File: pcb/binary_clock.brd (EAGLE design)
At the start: 100 x 80 mm, 18 parts

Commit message: PCB almost done.
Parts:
- added C1: (no value), rcl:C0603K
- added R1, R2: (no value), rcl:R0603
- added S1: SET, SparkFun-Switches:TACTILE_SWITCH_SMD_5.2MM
- moved U$1 62.1 mm to (17.8, 52.1), flipped to the bottom, turned to 90 degrees
- moved D11 38.1 mm to (14.0, 55.9), turned to 90 degrees
- moved D6 38.1 mm to (52.1, 55.9), turned to 90 degrees
- moved D10 22.9 mm to (21.6, 55.9), turned to 90 degrees
- moved D7 22.9 mm to (44.5, 55.9), turned to 90 degrees
- moved D4 7.62 mm to (44.5, 63.5)
- moved D2 7.62 mm to (29.2, 63.5)
- moved D1 7.62 mm to (21.6, 63.5)
- moved D3 7.62 mm to (36.8, 63.5)
- moved D5 7.62 mm to (52.1, 63.5)
- moved D8 7.62 mm to (36.8, 55.9), turned to 90 degrees
- moved D9 7.62 mm to (29.2, 55.9), turned to 90 degrees
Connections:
- new net LED_CK: R1.1, U$1.6
- new net LED_D: R2.1, U$1.5
- new net N$31: D17.P6
- new net N$32: U$1.1
- new net N$33: U$1.3
- new net N$34: D17.P5
- new net N$35: U$1.2
- new net N$36: U$1.7
- new net N$41: D1.P1, R2.2
- new net N$42: D1.P2, R1.2
- new net SW: S1.1, S1.2
- net +5V: now also C1.1
- net GND: now also C1.2, S1.3, S1.4
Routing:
- net GND: track 0.00 -> 110.6 mm, vias 0 -> 17
- net +5V: track 0.00 -> 63.3 mm, vias 0 -> 17
- net N$38: track 48.3 -> 10.9 mm
- net N$37: track 42.3 -> 16.3 mm
- net N$20: track 0.00 -> 10.9 mm
- net LED_CK: track 0.00 -> 8.92 mm
- net N$41: track 0.00 -> 6.81 mm, vias 0 -> 1
- net LED_D: track 0.00 -> 5.14 mm
- net N$19: track 0.00 -> 4.95 mm
- net N$42: track 0.00 -> 4.67 mm, vias 0 -> 1

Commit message: Switch connected
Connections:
- removed net N$36: U$1.7
- net SW: now also U$1.7
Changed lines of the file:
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@@
 <contactref element="U$1" pad="2"/>
-</signal>
-<signal name="N$36">
-<contactref element="U$1" pad="7"/>
 </signal>
 <signal name="LED_D">
@@
 <contactref element="S1" pad="2"/>
 <contactref element="S1" pad="1"/>
+<contactref element="U$1" pad="7"/>
 <wire x1="11.176" y1="65.405" x2="16.764" y2="65.405" width="0" layer="19" extent="1-1"/>
+<wire x1="20.934" y1="51.435" x2="16.764" y2="65.405" width="0" layer="19" extent="1-16"/>
 </signal>
 </signals>

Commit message: Routing done.
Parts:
- added R3: (no value), rcl:R0603
- added Y1: OSCILLATORSMD-5X3, SparkFun-Clocks:OSCILLATOR-SMD-5X3.2
- moved C1 12.8 mm to (16.8, 54.9)
- moved U$1 7.62 mm to (25.4, 52.1)
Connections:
- new net N$36: R3.2, S1.1, S1.2
- net +5V: now also Y1.4
- net GND: now also Y1.2
- net N$35: now also Y1.3
- net SW: now also R3.1; no longer S1.1, S1.2
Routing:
- net +5V: track 63.3 -> 144.7 mm, vias 17 -> 19
- net GND: track 110.6 -> 138.7 mm, vias 17 -> 18
- net N$36: track 0.00 -> 18.0 mm, vias 0 -> 1
- net SW: track 0.00 -> 13.3 mm
- net LED_CK: track 8.92 -> 14.2 mm
- net LED_D: track 5.14 -> 9.78 mm
- net N$35: track 0.00 -> 4.35 mm
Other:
- outline, holes or cut-outs redrawn
- board text added: "+"
- board text added: "-"

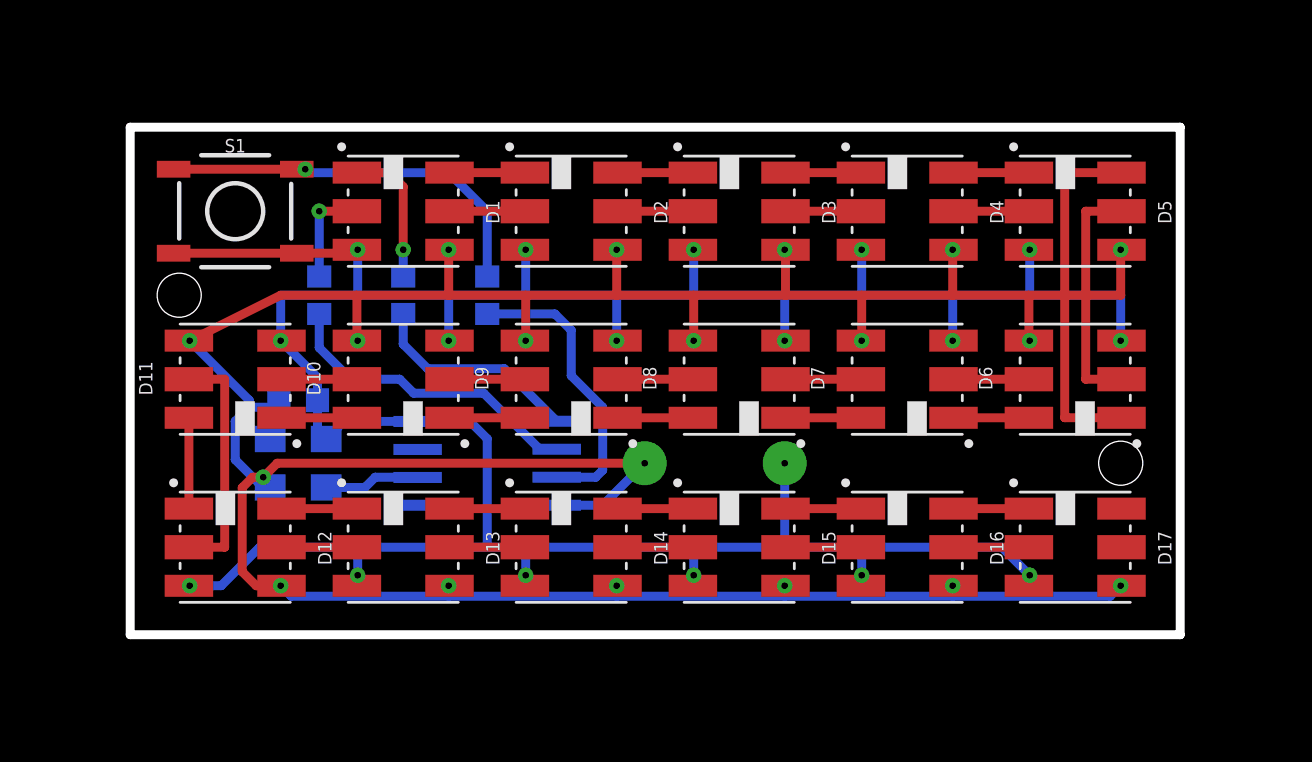
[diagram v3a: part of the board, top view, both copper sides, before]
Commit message: Silkscreen and resistor sizes
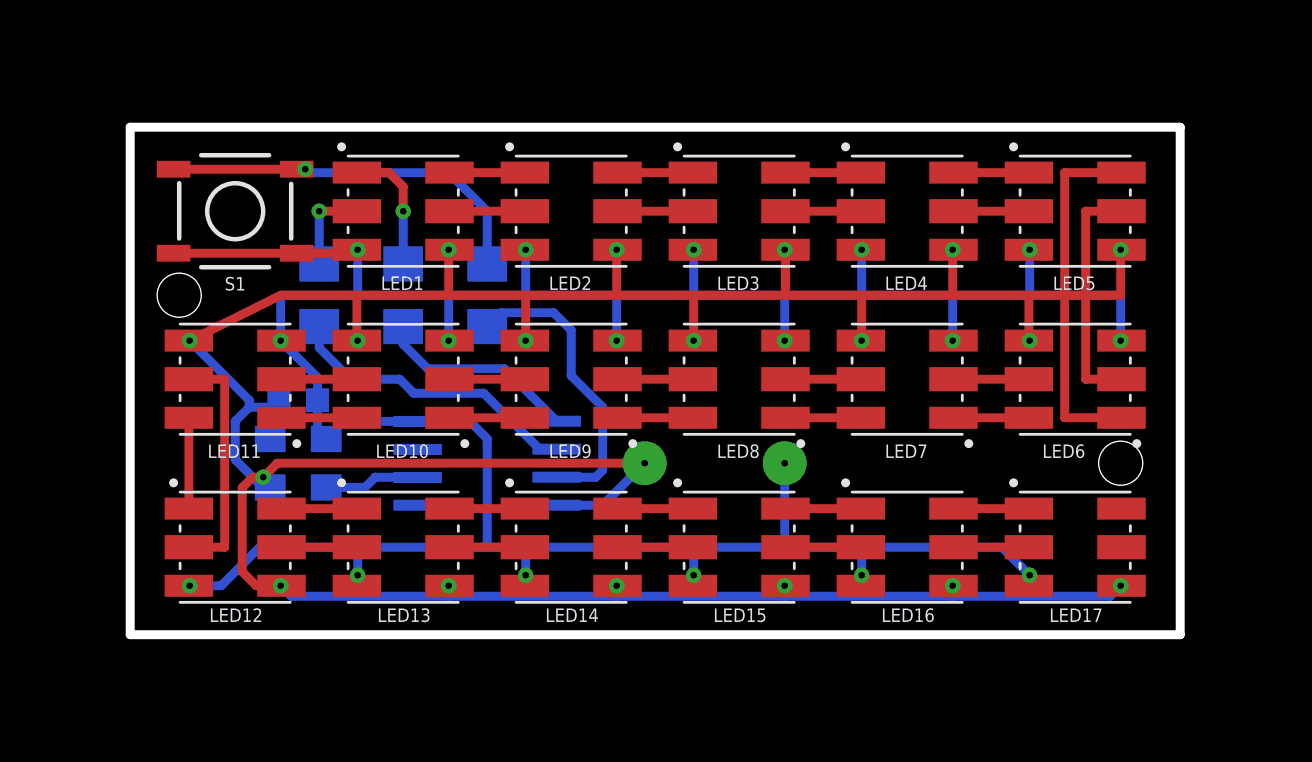
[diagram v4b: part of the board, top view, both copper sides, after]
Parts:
- R1, R2, R3: device rcl:R0603 -> rcl:R1206
- renumbered D1 to LED1, D10 to LED10, D11 to LED11, D12 to LED12, D13 to LED13, D14 to LED14, D15 to LED15, D16 to LED16, D17 to LED17, D2 to LED2, D3 to LED3, D4 to LED4, D5 to LED5, D6 to LED6, D7 to LED7, D8 to LED8, D9 to LED9, U$1 to MCU, Y1 to OSC
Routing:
- net N$42: track 4.67 -> 4.10 mm
- net N$41: track 6.44 -> 5.86 mm
- net N$36: track 18.0 -> 17.4 mm
- net LED_D: track 9.78 -> 9.21 mm
- net LED_CK: track 14.2 -> 13.6 mm

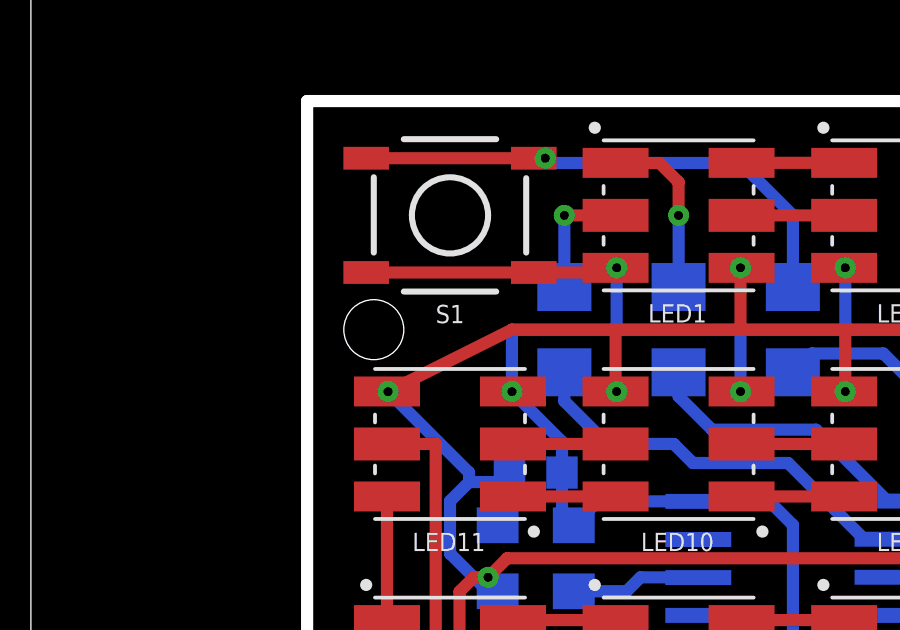
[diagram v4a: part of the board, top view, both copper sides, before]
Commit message: Switch renamed
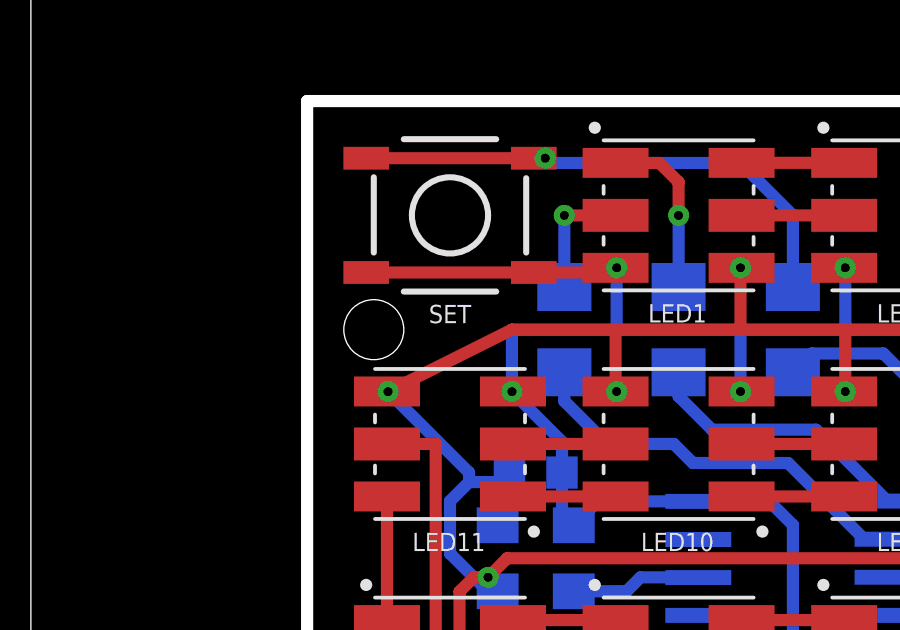
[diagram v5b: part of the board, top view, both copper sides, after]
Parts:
- renumbered S1 to SET
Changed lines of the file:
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@@
 <layer number="19" name="Unrouted" color="6" fill="1" visible="yes" active="yes"/>
 <layer number="20" name="Dimension" color="15" fill="1" visible="yes" active="yes"/>
-<layer number="21" name="tPlace" color="7" fill="1" visible="no" active="yes"/>
-<layer number="22" name="bPlace" color="7" fill="1" visible="yes" active="yes"/>
-<layer number="23" name="tOrigins" color="15" fill="1" visible="no" active="yes"/>
-<layer number="24" name="bOrigins" color="15" fill="1" visible="yes" active="yes"/>
-<layer number="25" name="tNames" color="7" fill="1" visible="no" active="yes"/>
-<layer number="26" name="bNames" color="7" fill="1" visible="yes" active="yes"/>
+<layer number="21" name="tPlace" color="7" fill="1" visible="yes" active="yes"/>
+<layer number="22" name="bPlace" color="7" fill="1" visible="no" active="yes"/>
+<layer number="23" name="tOrigins" color="15" fill="1" visible="yes" active="yes"/>
+<layer number="24" name="bOrigins" color="15" fill="1" visible="no" active="yes"/>
+<layer number="25" name="tNames" color="7" fill="1" visible="yes" active="yes"/>
+<layer number="26" name="bNames" color="7" fill="1" visible="no" active="yes"/>
 <layer number="27" name="tValues" color="7" fill="1" visible="no" active="yes"/>
 <layer number="28" name="bValues" color="7" fill="1" visible="no" active="yes"/>
@@
 <attribute name="VALUE" x="23.241" y="56.134" size="1.27" layer="28" ratio="10" rot="MR180"/>
 </element>
-<element name="S1" library="SparkFun-Switches" package="TACTILE_SWITCH_SMD_5.2MM" value="SET" x="13.97" y="63.5" smashed="yes">
+<element name="SET" library="SparkFun-Switches" package="TACTILE_SWITCH_SMD_5.2MM" value="SET" x="13.97" y="63.5" smashed="yes">
 <attribute name="SF_SKU" value="COM-08720" x="13.97" y="63.5" size="1.778" layer="27" display="off"/>
 <attribute name="PROD_ID" value="SWCH-08247" x="13.97" y="63.5" size="1.778" layer="27" display="off"/>
@@
 <wire x1="54.13375" y1="57.62625" x2="54.13375" y2="59.69" width="0.4064" layer="16"/>
 <wire x1="54.13375" y1="59.69" x2="50.00625" y2="59.69" width="0.4064" layer="16"/>
-<contactref element="S1" pad="3"/>
-<contactref element="S1" pad="4"/>
+<contactref element="SET" pad="3"/>
+<contactref element="SET" pad="4"/>
 <contactref element="C1" pad="2"/>
 <wire x1="16.764" y1="61.595" x2="19.52625" y2="61.595" width="0.4064" layer="1"/>
@@
 </signal>
 <signal name="N$36">
-<contactref element="S1" pad="1"/>
-<contactref element="S1" pad="2"/>
+<contactref element="SET" pad="1"/>
+<contactref element="SET" pad="2"/>
 <contactref element="R3" pad="2"/>
 <wire x1="11.176" y1="65.405" x2="16.764" y2="65.405" width="0.4064" layer="1"/>

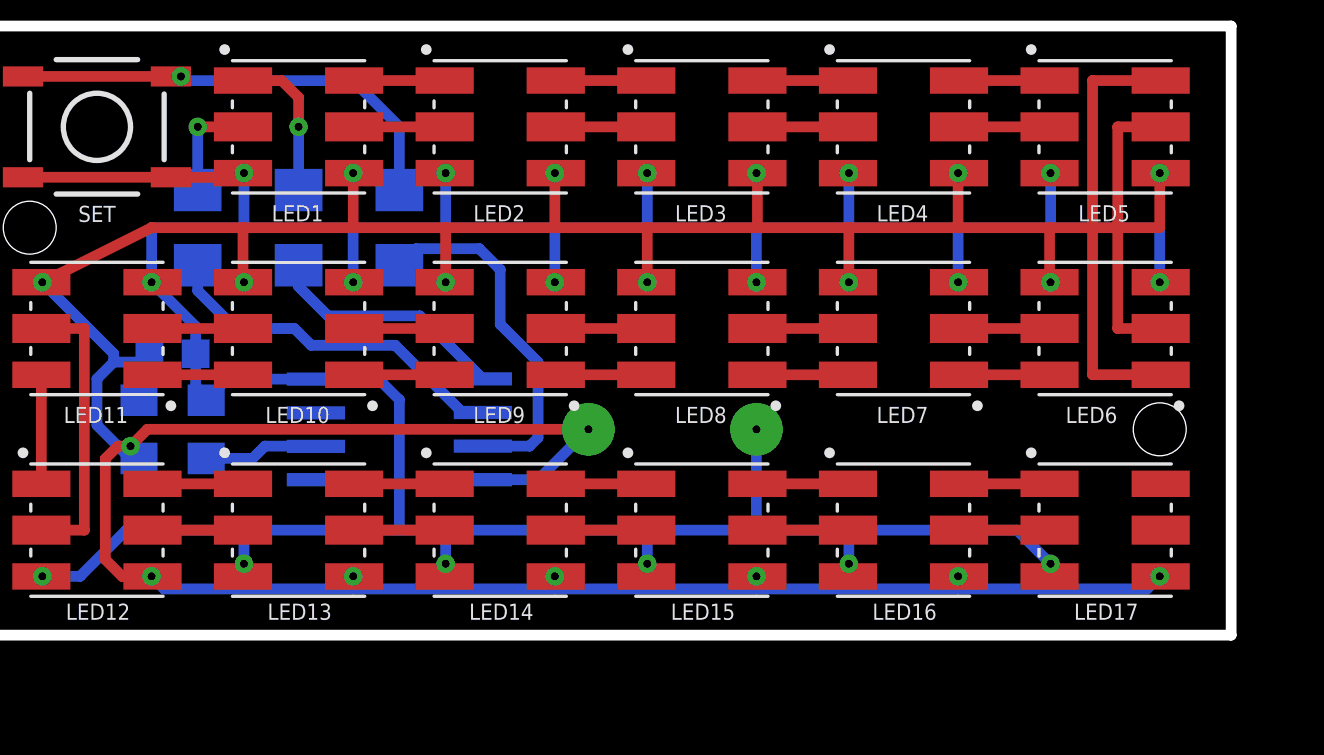
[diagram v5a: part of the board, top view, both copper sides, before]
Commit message: More 100nFs added, short circuit corrected, text added
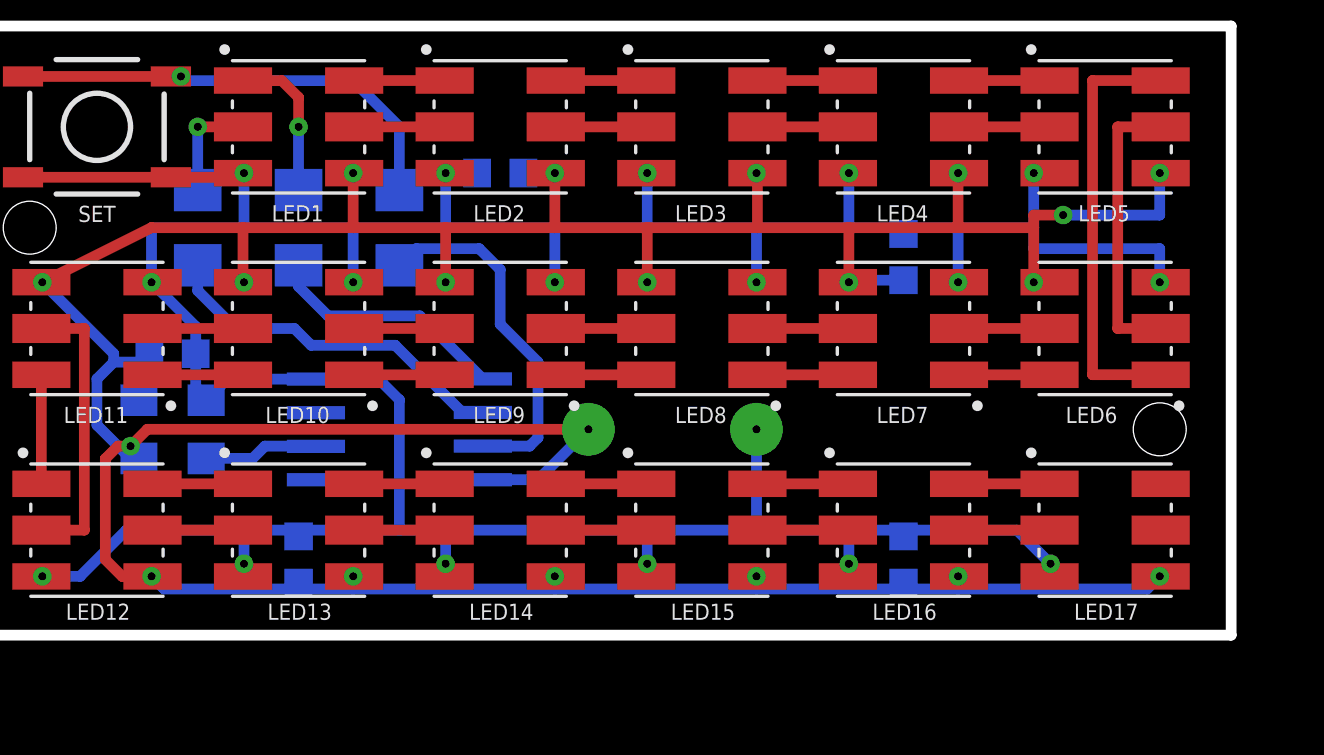
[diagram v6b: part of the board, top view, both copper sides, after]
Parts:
- added C2, C3, C4, C5: (no value), rcl:C0603K
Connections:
- net +5V: now also C2.1, C3.1, C4.1, C5.1
- net GND: now also C2.2, C3.2, C4.2, C5.2
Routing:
- net +5V: track 144.7 -> 149.2 mm, vias 19 -> 20
- net GND: track 138.7 -> 141.8 mm
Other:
- board text added: "ElectrIT Binary clock"

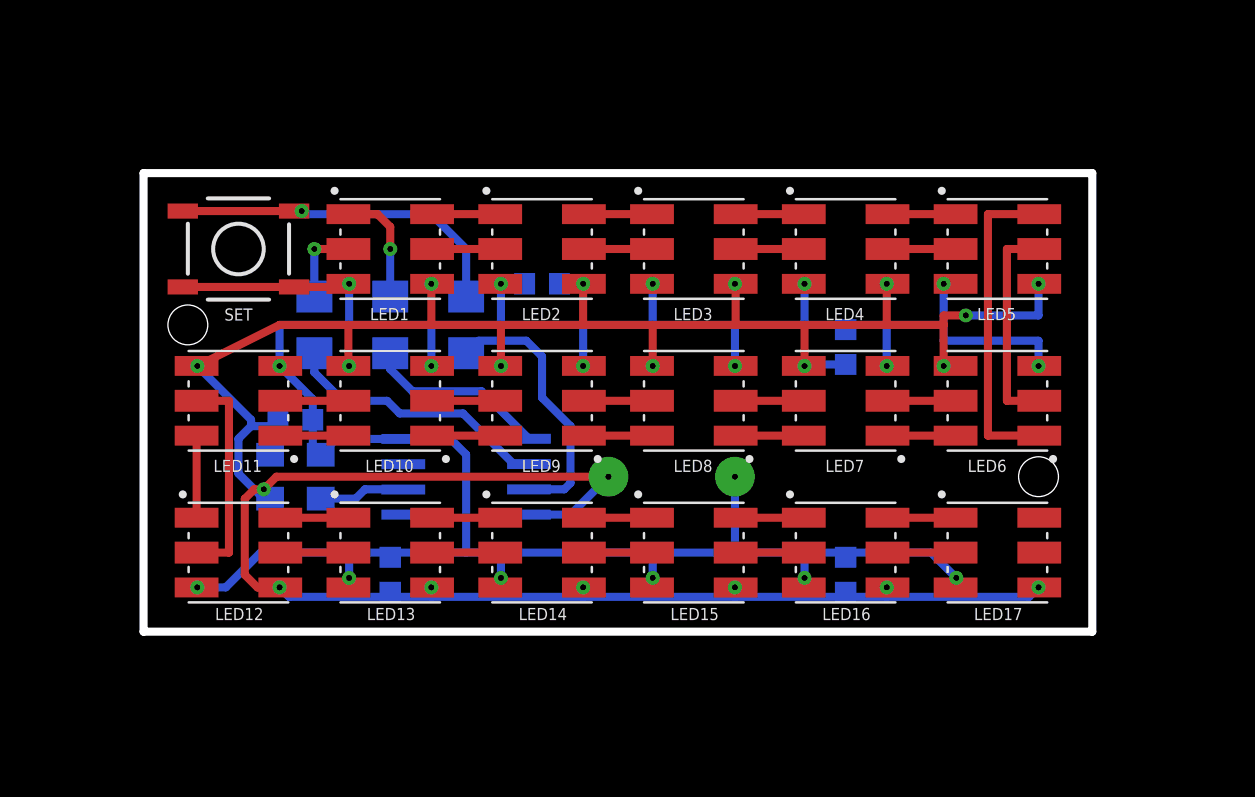
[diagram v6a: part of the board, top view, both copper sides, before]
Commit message: Font sizes and positions corrected
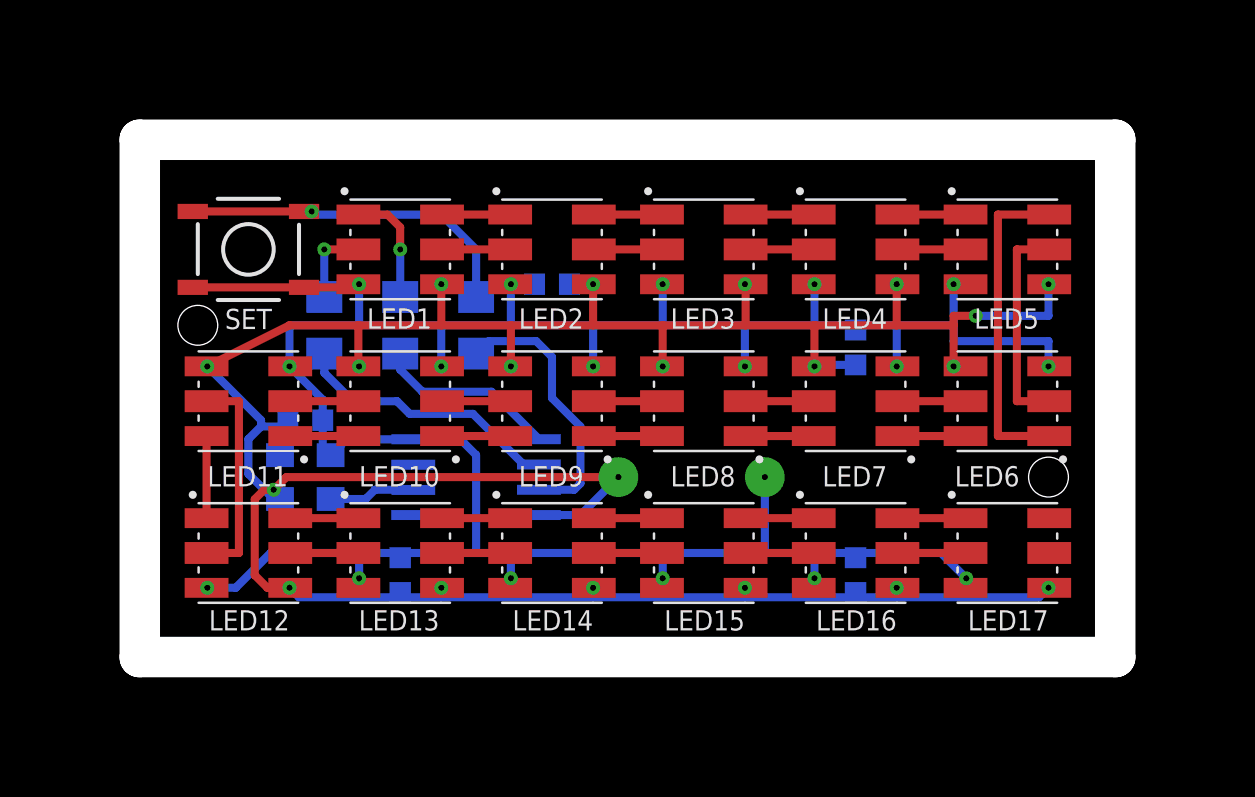
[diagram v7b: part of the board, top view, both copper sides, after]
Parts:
- moved C1 0.50 mm to (17.3, 54.9)
- moved C2 0.50 mm to (22.1, 47.1)
- moved C3 0.50 mm to (45.0, 47.1)
- moved LED1 0.50 mm to (22.1, 63.5)
- moved LED10 0.50 mm to (22.1, 55.9)
- moved LED11 0.50 mm to (14.5, 55.9)
- moved LED2 0.50 mm to (29.7, 63.5)
- moved LED3 0.50 mm to (37.3, 63.5)
- moved LED4 0.50 mm to (45.0, 63.5)
- moved LED5 0.50 mm to (52.6, 63.5)
- moved LED6 0.50 mm to (52.6, 55.9)
- moved LED7 0.50 mm to (45.0, 55.9)
- moved LED8 0.50 mm to (37.3, 55.9)
- moved LED9 0.50 mm to (29.7, 55.9)
- moved MCU 0.50 mm to (25.9, 52.0)
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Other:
- outline, holes or cut-outs redrawn
